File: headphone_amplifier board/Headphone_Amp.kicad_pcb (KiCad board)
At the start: 4 copper layers, 111.7 x 81.2 mm, 145 parts, among them J1 PWR_IN, J2 Headphone_IN, J3 Audio_IN, J4 Conn_01x03, J5 Conn_01x03, T1 SSM3J338R_LF, U1 NE5532, U10 NE5532, U11 NE5532, U12 NE5532, U13 NE5532, U14 NE5532, U15 NE5532, U16 NE5532, U17 NE5532, U18 NE5532, U19 LM317_TO-252, U2 NE5532, U3 NE5532, U4 NE5532, U5 NE5532, U6 NE5532, U7 NE5532, U8 NE5532, U9 NE5532

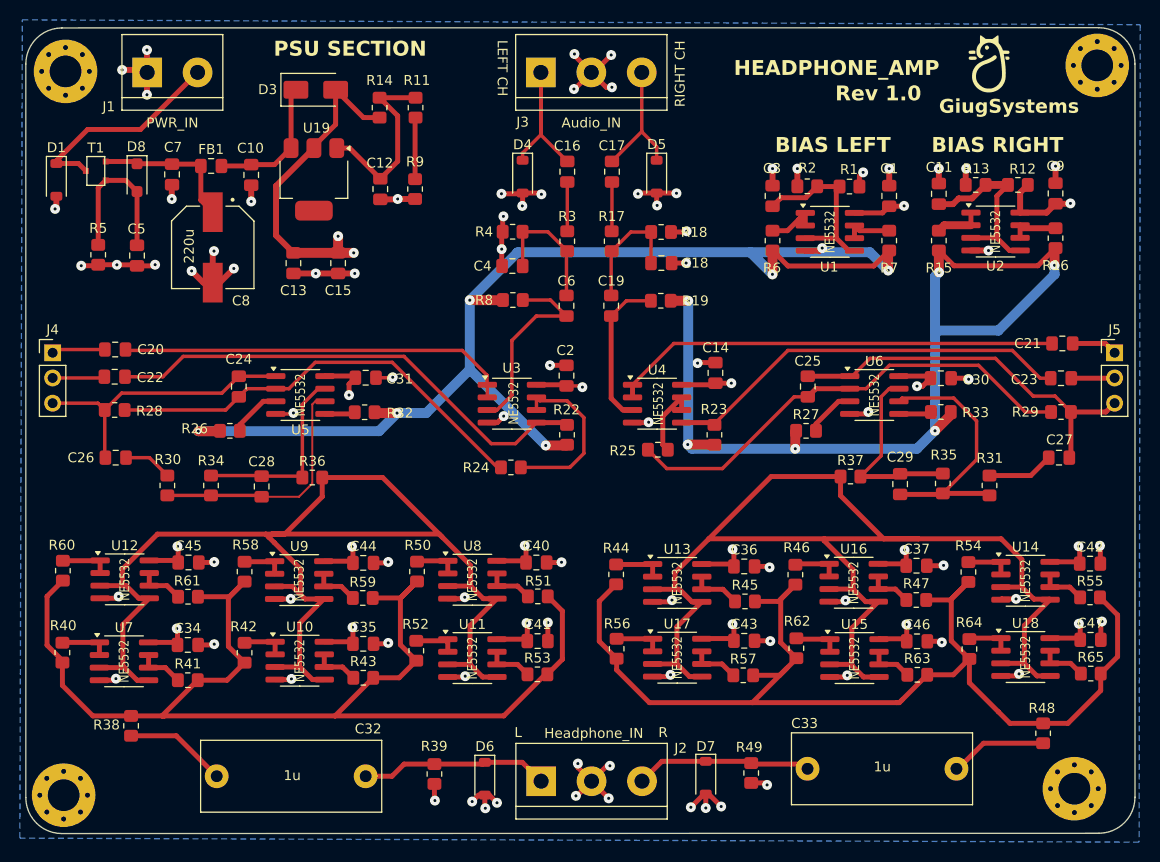
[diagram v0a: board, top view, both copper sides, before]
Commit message: revisited bias plane
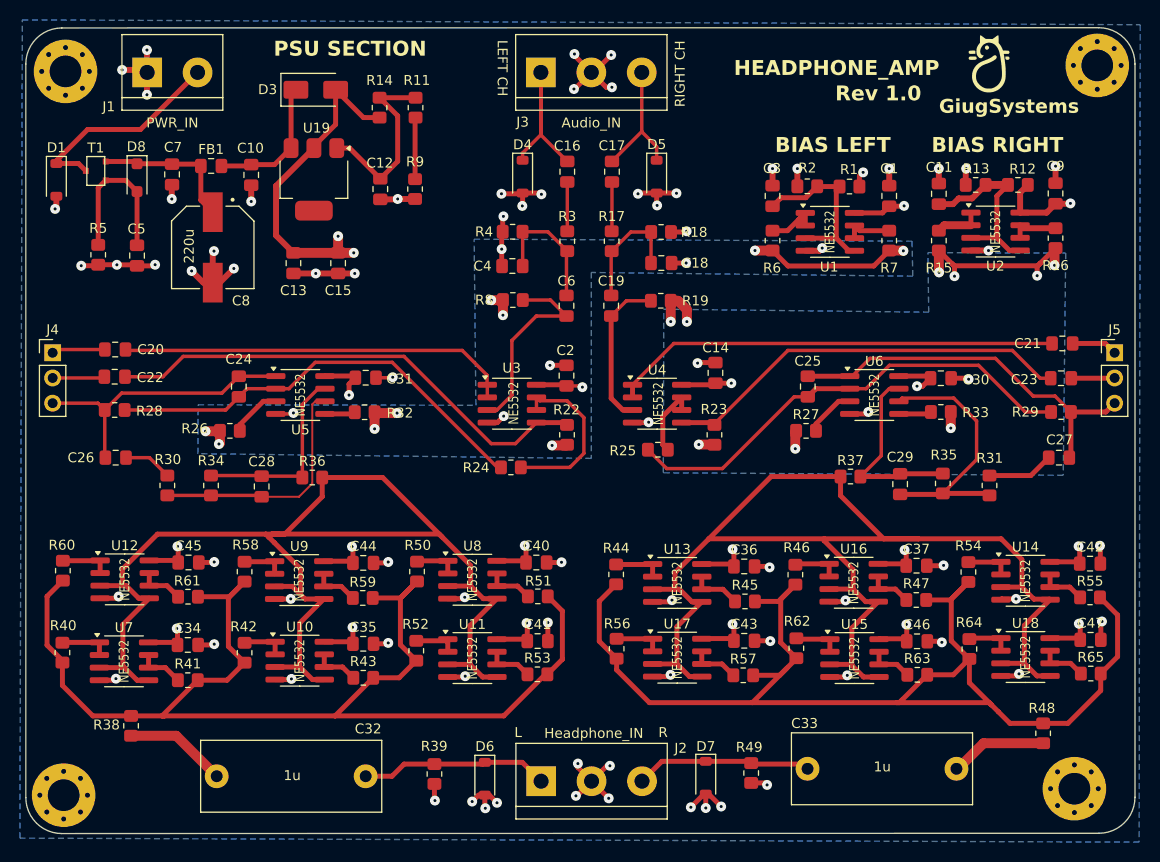
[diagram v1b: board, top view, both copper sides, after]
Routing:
- net VBIAS_LEFT: track 123.2 -> 27.3 mm, vias 6 -> 9
- net VBIAS_RIGHT: track 97.7 -> 30.2 mm, vias 6 -> 9
- net DRIVER_OUT_RIGHT: track 116.0 -> 125.6 mm
- added copper zone on B.Cu, net VBIAS_LEFT
- added copper zone on B.Cu, net VBIAS_RIGHT
